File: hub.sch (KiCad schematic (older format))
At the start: 33 parts, among them IC1 SN65220DBVT, IC2 TUSB2046IBVF, Y1 6Mhz

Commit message: deleted all, beginning of eval board
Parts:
- removed C1, C6: 10 uF, SamacSys_Parts:CAPC3216X180N, symbol SamacSys_Parts:CL31A106KPHNNNE
- removed C2, C4, C7: 0.1 uF, SamacSys_Parts:CAPC3216X88N, symbol SamacSys_Parts:C1206C104K5RAC7411
- removed C3, C5: 27 pF, SamacSys_Parts:CAPC3216X170N, symbol SamacSys_Parts:VJ1206A270JXBAC
- removed IC1: SN65220DBVT, SamacSys_Parts:SOT95P280X145-6N, symbol SamacSys_Parts:SN65220DBVT
- removed R1, R12, R15, R17, R18, R19, R2, R20, R7, R9: 22, SamacSys_Parts:RESC3116X70N, symbol SamacSys_Parts:ERJ-8ENF22R0V
- removed R10, R13, R16, R21, R22, R23, R5, R8: 15K, SamacSys_Parts:RESC3216X75N, symbol SamacSys_Parts:CR1206-FX-1502ELF
- removed R11, R4: 1K5, SamacSys_Parts:RESC2012X60N, symbol SamacSys_Parts:ERA-6AED152V
- removed R14, R6: 4K7, SamacSys_Parts:RESC3116X65N, symbol SamacSys_Parts:CRGCQ1206F4K7
- removed R3: 10K, SamacSys_Parts:RESC3216X60N, symbol SamacSys_Parts:CRCW120610K0FKEAC
- removed Y1: 6Mhz, SamacSys_Parts:LFXTAL036567BULK, symbol SamacSys_Parts:LFXTAL036567BULK
- added C1: 1uF, symbol Device:C_Small
- added C2, C3: 22pF, symbol Device:C_Small
- added C4: 2.2uF, symbol Device:C_Small
- added C5: 0.1uF, symbol Device:C_Small
- added C6: 4.7uF, symbol Device:CP_Small
- added IC5: TPD2E2U06DCKR, SOT65P210X110-3N, symbol SamacSys_Parts:TPD2E2U06DCKR
- added IC6: TLV76733DGNR, SOP65P490X110-9N, symbol SamacSys_Parts:TLV76733DGNR
- added J1: USB_B_Micro, symbol Connector:USB_B_Micro
- added J? (x2): 10129381-906001BLF, HDRV6W67P254_2X3_762X483X858P, symbol SamacSys_Parts:10129381-906001BLF
- added R1: 33, symbol Device:R_Small
- added R2, R3: 22, symbol Device:R_Small
- added R4: 1.5k, symbol Device:R_Small
- added TP1: TestPoint, symbol Connector:TestPoint
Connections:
- net +3V3: now also J?.2, J?.4, J?.6, R4.2; no longer IC2.25 (VCC_2), IC2.3 (VCC_1)
- net GND: now also C1.2, C2.2, C3.2, C4.2, C5.2, C6.2, IC5.3 (GND), IC6.4 (GND_1), IC6.6 (GND_2), IC6.9 (EP), J1.6 (Shield), R1.2; no longer IC2.27 (TSTPLL/48MCLK), IC2.28 (GND_2), IC2.31 (TSTMODE), IC2.6 (EEDATA/GANGED), IC2.7 (GND_1), IC2.8 (BUSPWR)
- new net: IC5.1 (IO1), J1.2 (D-), R3.2
- new net: IC5.2 (IO2), J1.3 (D+), R2.2
- new net: J1.5 (GND), R1.1
- new net: IC6.5 (EN), TP1.1
- new net 3V3_Buck_1: C4.1, IC6.1 (OUT), IC6.2 (SNS), J?.1
- new net Buck_1: C1.1, IC6.8 (IN), J?.2
- new net Buck_2: J?.4
- new net DMO: C2.1, R3.1
- new net DP0: C3.1, R2.1, R4.1
- new net LDO: J?.6
- new net VBUS: C5.1, C6.1, J1.1 (VBUS), J?.1, J?.3, J?.5
- now unconnected: IC2.10 (~OVRCUR1), IC2.14 (~OVRCUR2), IC2.18 (~OVRCUR3), IC2.22 (~OVRCUR4)
- no-connect marks 0 -> 3
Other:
- note added: "Buck_1"
- note added: "Microusb B Connector - upstream\n\n"
- note added: "Power Switches"
- moved on the sheet: IC2

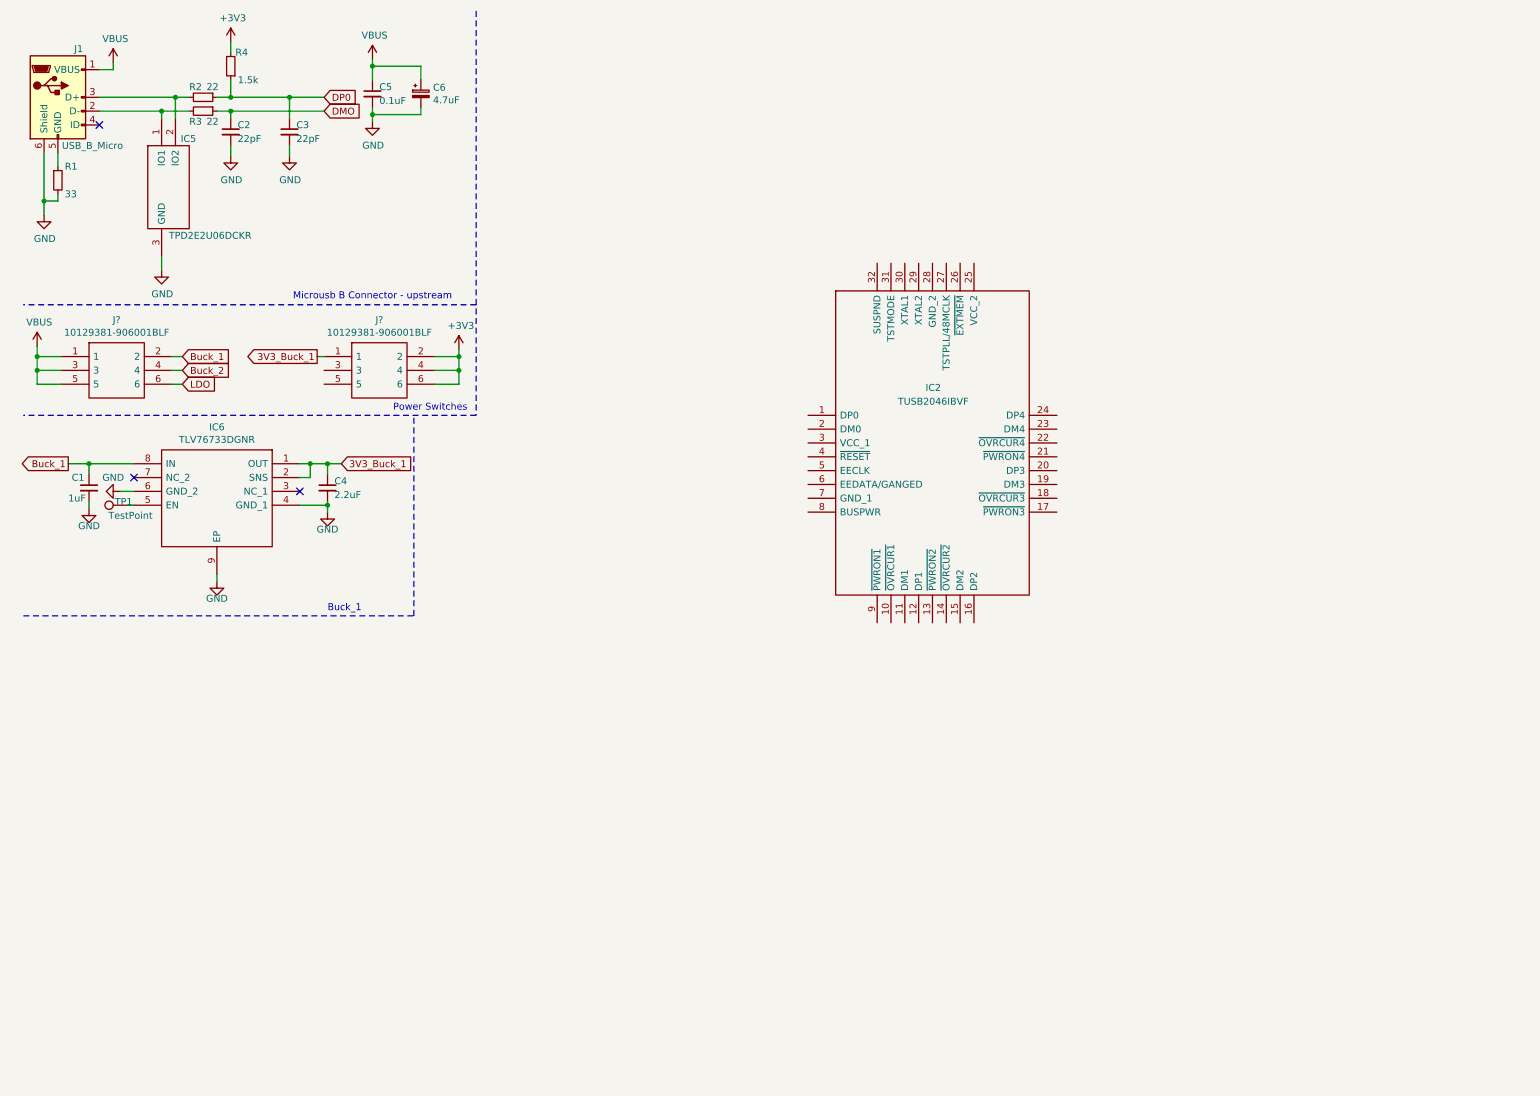
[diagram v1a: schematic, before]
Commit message: hub schematic finished
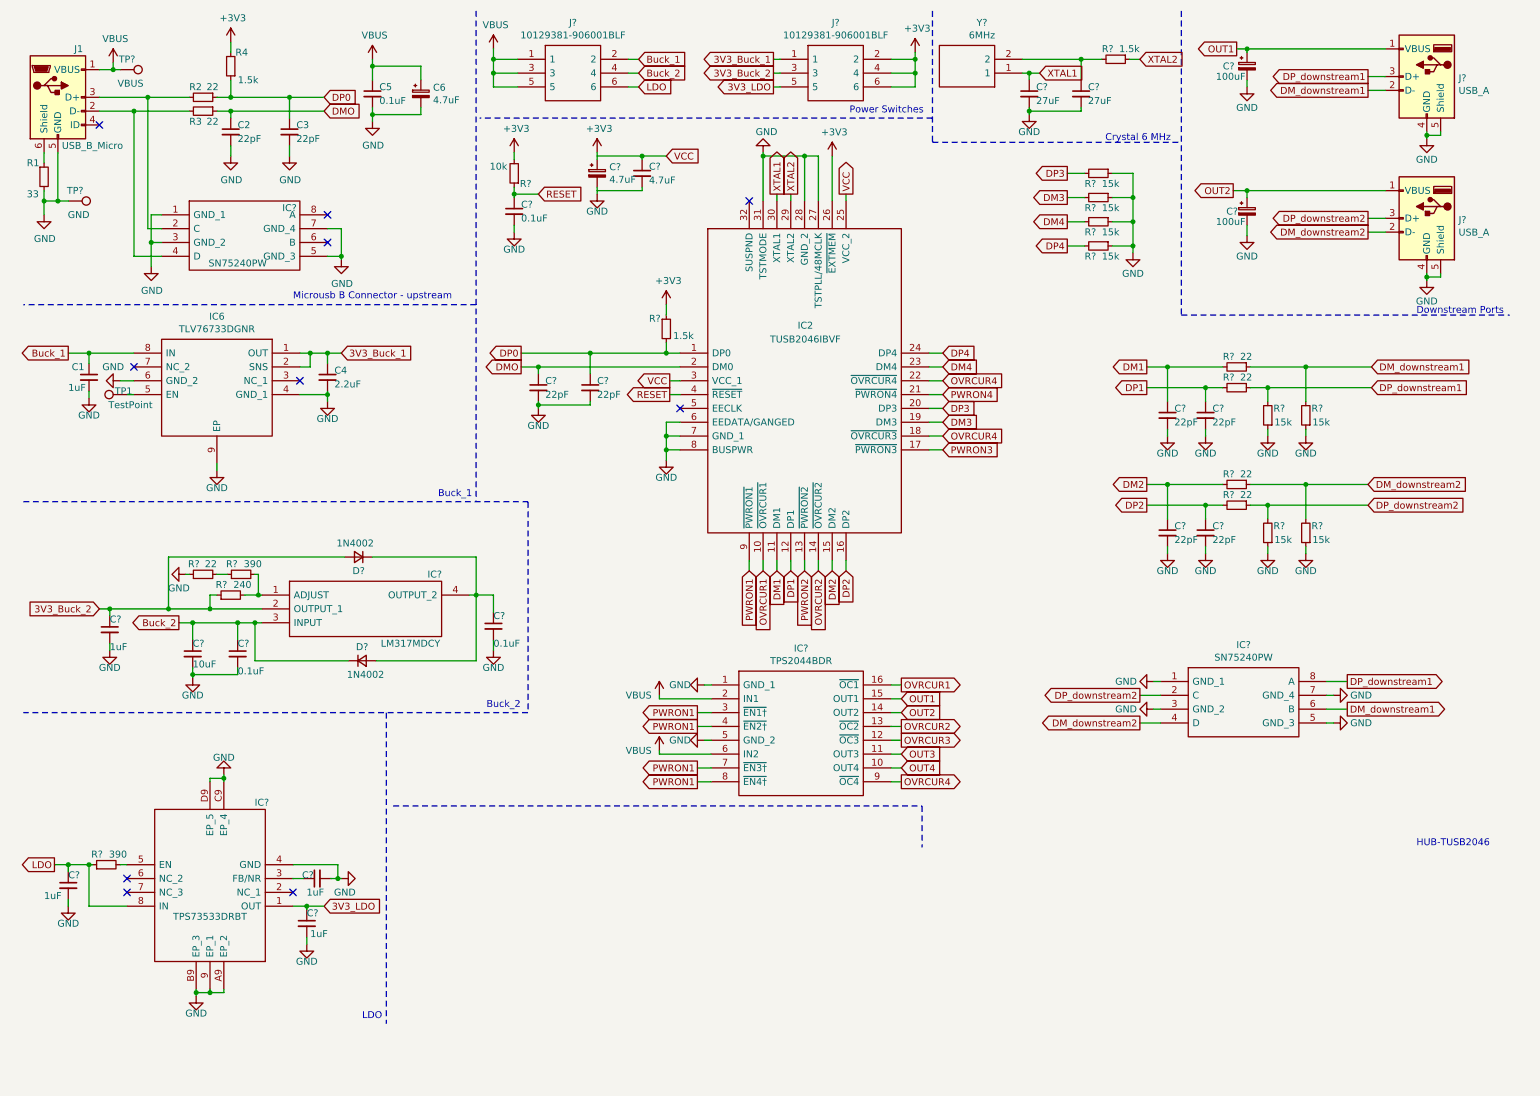
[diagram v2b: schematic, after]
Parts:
- removed IC5: TPD2E2U06DCKR, SOT65P210X110-3N, symbol SamacSys_Parts:TPD2E2U06DCKR
- added C?: 10uF, symbol Device:C_Small
- added C? (x3): 0.1uF, symbol Device:C_Small
- added C? (x4): 1uF, symbol Device:C_Small
- added C? (x6): 22pF, symbol Device:C_Small
- added C?: 4.7uF, symbol Device:C_Small
- added C? (x2): 27uF, symbol Device:C_Small
- added C?: 4.7uF, symbol Device:CP_Small
- added C? (x2): 100uF, symbol Device:CP_Small
- added D? (x2): 1N4002, symbol Device:D_Small
- added IC?: LM317MDCY, SOT230P700X180-4N, symbol SamacSys_Parts:LM317MDCY
- added IC?: TPS73533DRBT, TPS73533DRBT, symbol SamacSys_Parts:TPS73533DRBT
- added IC?: TPS2044BDR, SOIC127P600X175-16N, symbol SamacSys_Parts:TPS2044BDR
- added IC? (x2): SN75240PW, SOP65P640X120-8N, symbol SamacSys_Parts:SN75240PW
- added J? (x2): USB_A, symbol Connector:USB_A
- added R?: 240, symbol Device:R_Small
- added R? (x5): 22, symbol Device:R_Small
- added R? (x2): 390, symbol Device:R_Small
- added R? (x2): 1.5k, symbol Device:R_Small
- added R?: 10k, symbol Device:R_Small
- added R? (x8): 15k, symbol Device:R_Small
- added TP?: VBUS, symbol Connector:TestPoint
- added TP?: GND, symbol Connector:TestPoint
- added Y?: 6MHz, LFXTAL036567BULK, symbol SamacSys_Parts:LFXTAL036567BULK
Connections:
- net +3V3: now also IC2.26 (~EXTMEM), C?.1, R?.1, R?.2
- net Buck_2: now also C?.1, C?.1, D?.1 (K), IC?.3 (INPUT)
- net DMO: now also IC2.2 (DM0), C?.1
- net DP0: now also IC2.1 (DP0), C?.1, R?.2
- net GND: now also IC2.27 (TSTPLL/48MCLK), IC2.28 (GND_2), IC2.31 (TSTMODE), IC2.6 (EEDATA/GANGED), IC2.7 (GND_1), IC2.8 (BUSPWR), J1.5 (GND), C?.2, C?.2, C?.2, C?.2, C?.2, C?.2, C?.2, C?.2, C?.2, C?.2, C?.2, C?.2, C?.2, C?.2, C?.2, C?.2, C?.2, C?.2, C?.2, IC?.1 (GND_1), IC?.1 (GND_1), IC?.1 (GND_1), IC?.3 (GND_2), IC?.3 (GND_2), IC?.4 (GND), IC?.5 (GND_2), IC?.5 (GND_3), IC?.5 (GND_3), IC?.7 (GND_4), IC?.7 (GND_4), IC?.9 (EP_1), IC?.A9 (EP_2), IC?.B9 (EP_3), IC?.C9 (EP_4), IC?.D9 (EP_5), J?.4 (GND), J?.4 (GND), J?.5 (Shield), J?.5 (Shield), R?.1, R?.1, R?.1, R?.1, R?.1, R?.1, R?.1, R?.1, R?.1, TP?.1; no longer J1.6 (Shield)
- net LDO: now also C?.1, IC?.8 (IN), R?.1
- net VBUS: now also IC?.2 (IN1), IC?.6 (IN2), TP?.1
- net OVRCUR1: now reaches IC2.10 (~OVRCUR1)
- net OVRCUR1: now also IC?.16 (~OC1)
- net DM1: now reaches IC2.11 (DM1)
- net DM1: now also C?.1, R?.2
- net DP1: now reaches IC2.12 (DP1)
- net DP1: now also C?.1, R?.2
- net PWRON2: now reaches IC2.13 (~PWRON2)
- net OVRCUR2: now reaches IC2.14 (~OVRCUR2)
- net OVRCUR2: now also IC?.13 (~OC2)
- net DM2: now reaches IC2.15 (DM2)
- net DM2: now also C?.1, R?.2
- net DP2: now reaches IC2.16 (DP2)
- net DP2: now also C?.1, R?.2
- net PWRON3: now reaches IC2.17 (~PWRON3)
- net OVRCUR4: now reaches IC2.18 (~OVRCUR3)
- net OVRCUR4: now also IC2.22 (~OVRCUR4), IC?.9 (~OC4)
- net DM3: now reaches IC2.19 (DM3)
- net DM3: now also R?.2
- net DP3: now reaches IC2.20 (DP3)
- net DP3: now also R?.2
- net PWRON4: now reaches IC2.21 (~PWRON4)
- net DM4: now reaches IC2.23 (DM4)
- net DM4: now also R?.2
- net DP4: now reaches IC2.24 (DP4)
- net DP4: now also R?.2
- net VCC: now reaches IC2.25 (VCC_2)
- net VCC: now also IC2.3 (VCC_1), C?.1
- net XTAL2: now reaches IC2.29 (XTAL2)
- net XTAL2: now also R?.1
- net XTAL1: now reaches IC2.30 (XTAL1)
- net XTAL1: now also C?.1, Y?.1
- net RESET: now reaches IC2.4 (~RESET)
- net RESET: now also C?.1, R?.1
- net PWRON1: now reaches IC2.9 (~PWRON1)
- net PWRON1: now also IC?.3 (~EN1†), IC?.4 (~EN2†), IC?.7 (~EN3†), IC?.8 (~EN4†)
- net at J1.2 (D-), R3.2: now also IC?.4 (D)
- net at J1.3 (D+), R2.2: now also IC?.2 (C)
- net at R1.1: now also J1.6 (Shield); no longer J1.5 (GND)
- net 3V3_Buck_2: now reaches J?.3
- net 3V3_Buck_2: now also C?.1, D?.2 (A), IC?.2 (OUTPUT_1), R?.1
- net 3V3_LDO: now reaches J?.5
- net 3V3_LDO: now also C?.1, IC?.1 (OUT)
- new net: IC?.1 (ADJUST), R?.2, R?.2
- new net: C?.1, D?.1 (K), D?.2 (A), IC?.4 (OUTPUT_2)
- new net: R?.1, R?.2
- new net: C?.1, IC?.3 (FB/NR)
- new net: IC?.5 (EN), R?.2
- new net: C?.1, R?.2, Y?.2
- new net DM_downstream1: IC?.6 (B), J?.2 (D-), R?.1, R?.2
- new net DM_downstream2: IC?.4 (D), J?.2 (D-), R?.1, R?.2
- new net DP_downstream1: IC?.8 (A), J?.3 (D+), R?.1, R?.2
- new net DP_downstream2: IC?.2 (C), J?.3 (D+), R?.1, R?.2
- new net OUT1: C?.1, IC?.15 (OUT1), J?.1 (VBUS)
- new net OUT2: C?.1, IC?.14 (OUT2), J?.1 (VBUS)
- new net OUT3: IC?.11 (OUT3)
- new net OUT4: IC?.10 (OUT4)
- new net OVRCUR3: IC?.12 (~OC3)
- no-connect marks 3 -> 10
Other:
- note added: "Buck_1\n"
- note added: "Buck_2\n"
- note added: "Crystal 6 MHz"
- note added: "Downstream Ports"
- note added: "HUB-TUSB2046"
- note added: "LDO"
- note removed: "Buck_1"
- moved on the sheet: C1, C4, IC2, IC6, J?, R1, TP1

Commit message: split in two boards from now on
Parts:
- added D3: Buck_1, SamacSys_Parts:LEDC3214X78N, symbol Device:LED_Small
- added D4: Buck_2, SamacSys_Parts:LEDC3214X78N, symbol Device:LED_Small
- added D5: LDO, SamacSys_Parts:LEDC3214X78N, symbol Device:LED_Small
- added H1, H2, H3, H4: MountingHole_Pad, MountingHole:MountingHole_3.2mm_M3_Pad_Via, symbol Mechanical:MountingHole_Pad
- added R24, R? (x2): 1k, storage:R_1K, symbol Device:R_Small
- C1: footprint (none) -> storage:C_1uF
- C10, C13, C14: renamed from C?; footprint (none) -> storage:C_0.1uF
- C11, C12, C7, C8: renamed from C?; footprint (none) -> storage:C_1uF
- C15, C16, C21, C22, C23, C24: renamed from C?; footprint (none) -> storage:C_22pF
- C17, C18: renamed from C?; footprint (none) -> storage:C_4.7uF
- C19, C20: renamed from C?; footprint (none) -> storage:C_27pF
- C2, C3: footprint (none) -> storage:C_22pF
- C25, C26: renamed from C?; footprint (none) -> storage:C_100uF
- C4: footprint (none) -> storage:C_2.2F
- C5: footprint (none) -> storage:C_0.1uF
- C6: footprint (none) -> storage:C_4.7uF
- C9: renamed from C?; footprint (none) -> storage:C_10uF
- D1, D2: renamed from D?; footprint (none) -> storage:D_1N4002
- IC1, IC7: renamed from IC?; footprint SOP65P640X120-8N -> SamacSys_Parts:SOP65P640X120-8N
- IC3: renamed from IC?; footprint SOT230P700X180-4N -> SamacSys_Parts:SOT230P700X180-4N
- IC4: renamed from IC?; footprint TPS73533DRBT -> SamacSys_Parts:TPS73533DRBT
- IC5: renamed from IC?; footprint SOIC127P600X175-16N -> SamacSys_Parts:SOIC127P600X175-16N
- IC6: footprint SOP65P490X110-9N -> SamacSys_Parts:SOP65P490X110-9N
- J1: footprint (none) -> Connector_USB:USB_Micro-B_Molex-105017-0001
- J2, J3: renamed from J?; footprint HDRV6W67P254_2X3_762X483X858P -> SamacSys_Parts:HDRV6W67P254_2X3_762X483X858P
- J4, J5: renamed from J?; footprint (none) -> Connector_USB:USB_A_Molex_67643_Horizontal
- R1: value 33 -> 22; footprint (none) -> storage:R_22
- R10, R15: renamed from R?; footprint (none) -> storage:R_1K5
- R11, R12, R13, R14, R20, R21, R22, R23: renamed from R?; footprint (none) -> storage:R_15K
- R16, R17, R18, R19, R6: renamed from R?; footprint (none) -> storage:R_22
- R2, R3: footprint (none) -> storage:R_22
- R4: footprint (none) -> storage:R_1K5
- R5, R8: renamed from R?; footprint (none) -> storage:R_390
- R7: renamed from R?; footprint (none) -> storage:R_240
- R9: renamed from R?; footprint (none) -> storage:R_10K
- TP1: footprint (none) -> TestPoint:TestPoint_Pad_D2.5mm
- TP2, TP3: renamed from TP?; footprint (none) -> TestPoint:TestPoint_Pad_D2.5mm
- Y1: renamed from Y?; footprint LFXTAL036567BULK -> SamacSys_Parts:LFXTAL036567BULK
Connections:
- wire segments 301 -> 321
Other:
- note added: "LED-PowerSwichtes"
- note added: "Mountingholes"
